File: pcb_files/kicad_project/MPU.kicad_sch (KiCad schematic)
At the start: 12 parts, among them U2 MPU-6500

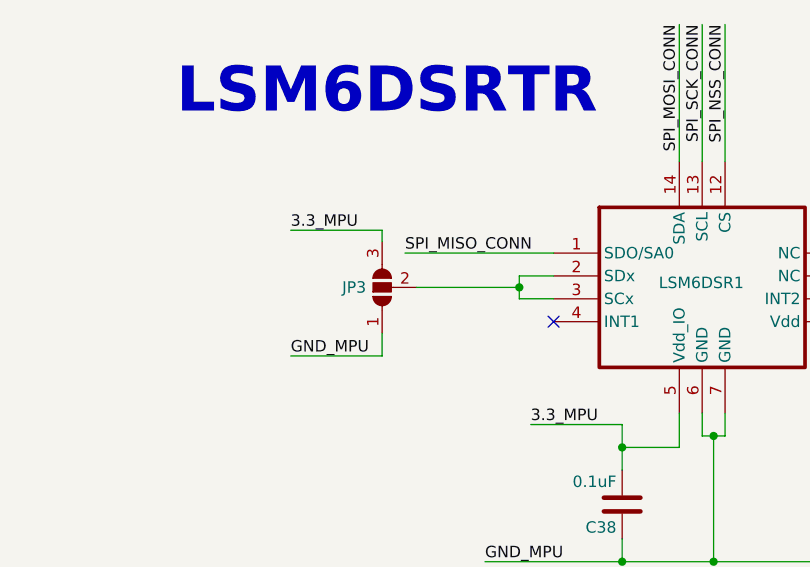
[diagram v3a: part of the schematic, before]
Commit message: Corrige errores de esquematico, crea las PCBs auxiliares, y posiciona todos los elementos para comenzar el ruteado.
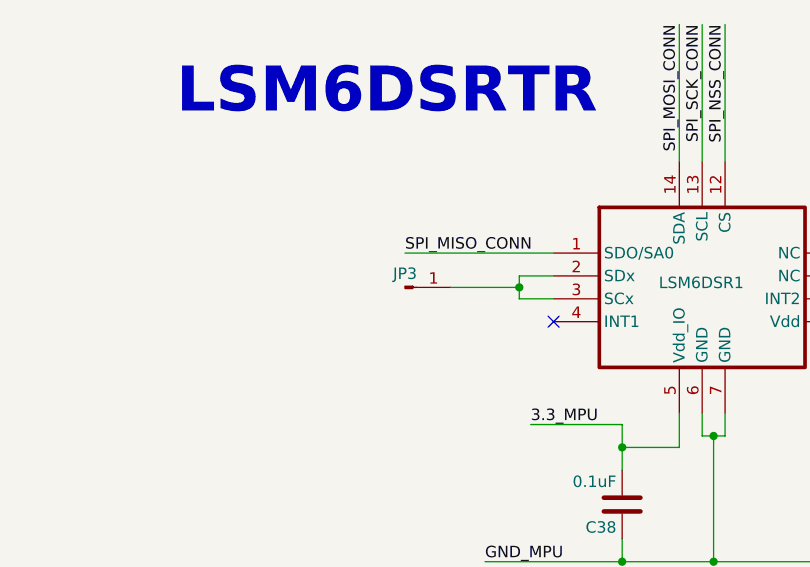
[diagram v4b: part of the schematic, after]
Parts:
- removed JP3: SolderJumper_3_Open, Jumper:SolderJumper-3_P1.3mm_Open_RoundedPad1.0x1.5mm, symbol Jumper:SolderJumper_3_Open
- added JP3: Conn_01x01_Pin, custom_footprints:Generic_simple_1x_SMD_pin, symbol Connector:Conn_01x01_Pin
- DATA_MPU2, DATA_MPU3: footprint custom_footprints:1x05 Pad -> custom_footprints:ZoroBot3_Data_MPU
- LSM6DSR1: footprint Sensor_Motion:Analog_LGA-16_3.25x3mm_P0.5mm_LayoutBorder3x5y -> Package_LGA:Bosch_LGA-14_3x2.5mm_P0.5mm
- POWER_MPU2, POWER_MPU3: footprint custom_footprints:1x05 Pad -> custom_footprints:ZoroBot3_Power_MPU
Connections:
- net at LSM6DSR1.2 (SDx), LSM6DSR1.3 (SCx): now also JP3.1 (Pin_1)
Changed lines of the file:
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@@
-	(wire
-		(pts
-			(xy 170.18 100.33) (xy 180.34 100.33)
-		)
-		(stroke
-			(width 0)
-			(type default)
-		)
-	)
 	(wire
 		(pts
@@
 	(wire
 		(pts
-			(xy 180.34 100.33) (xy 180.34 97.79)
-		)
-		(stroke
-			(width 0)
-			(type default)
-		)
-	)
-	(wire
-		(pts
 			(xy 217.17 109.22) (xy 217.17 123.19)
 		)
@@
 	(wire
 		(pts
-			(xy 180.34 86.36) (xy 180.34 87.63)
-		)
-		(stroke
-			(width 0)
-			(type default)
-		)
-	)
-	(wire
-		(pts
 			(xy 97.79 114.3) (xy 107.95 114.3)
 		)
@@
 	(wire
 		(pts
-			(xy 184.15 92.71) (xy 195.58 92.71)
+			(xy 187.96 92.71) (xy 195.58 92.71)
 		)
 		(stroke
@@
 		(pts
 			(xy 213.36 78.74) (xy 213.36 63.5)
-		)
-		(stroke
-			(width 0)
-			(type default)
-		)
-	)
-	(wire
-		(pts
-			(xy 180.34 86.36) (xy 170.18 86.36)
 		)
 		(stroke
@@
 		)
 	)
-	(label "3.3_MPU"
-		(at 170.18 86.36 0)
-		(fields_autoplaced yes)
-		(effects
-			(font
-				(size 1.27 1.27)
-			)
-			(justify left bottom)
-		)
-	)
 	(label "SPI_MOSI_CONN"
 		(at 142.24 128.27 180)
@@
 			)
 			(justify right bottom)
-		)
-	)
-	(label "GND_MPU"
-		(at 170.18 100.33 0)
-		(fields_autoplaced yes)
-		(effects
-			(font
-				(size 1.27 1.27)
-			)
-			(justify left bottom)
 		)
 	)
@@
 			)
 		)
-		(property "Footprint" "Sensor_Motion:Analog_LGA-16_3.25x3mm_P0.5mm_LayoutBorder3x5y"
+		(property "Footprint" "Package_LGA:Bosch_LGA-14_3x2.5mm_P0.5mm"
 			(at 215.9 93.98 0)
 			(effects
@@
 			)
 		)
-		(property "Footprint" "custom_footprints:1x05 Pad"
+		(property "Footprint" "custom_footprints:ZoroBot3_Power_MPU"
 			(at 120.65 115.57 0)
 			(effects
@@
 			)
 		)
-		(property "Footprint" "custom_footprints:1x05 Pad"
+		(property "Footprint" "custom_footprints:ZoroBot3_Data_MPU"
 			(at 248.92 127 0)
 			(effects
@@
 			)
 		)
-		(property "Footprint" "custom_footprints:1x05 Pad"
+		(property "Footprint" "custom_footprints:ZoroBot3_Data_MPU"
 			(at 120.65 128.27 0)
 			(effects
@@
 	)
 	(symbol
+		(lib_id "Connector:Conn_01x01_Pin")
+		(at 182.88 92.71 0)
+		(unit 1)
+		(exclude_from_sim no)
+		(in_bom yes)
+		(on_board yes)
+		(dnp no)
+		(property "Reference" "JP3"
+			(at 182.88 91.186 0)
+			(effects
+				(font
+					(size 1.27 1.27)
+				)
+			)
+		)
+		(property "Value" "Conn_01x01_Pin"
+			(at 183.642 93.98 0)
+			(effects
+				(font
+					(size 1.27 1.27)
+				)
+				(hide yes)
+			)
+		)
+		(property "Footprint" "custom_footprints:Generic_simple_1x_SMD_pin"
+			(at 182.88 92.71 0)
+			(effects
+				(font
+					(size 1.27 1.27)
+				)
+				(hide yes)
+			)
+		)
+		(property "Datasheet" "~"
+			(at 182.88 92.71 0)
+			(effects
+				(font
+					(size 1.27 1.27)
+				)
+				(hide yes)
+			)
+		)
+		(property "Description" "Generic connector, single row, 01x01, script generated"
+			(at 182.88 92.71 0)
+			(effects
+				(font
+					(size 1.27 1.27)
+				)
+				(hide yes)
+			)
+		)
+		(pin "1"
+		)
+		(instances
+			(project ""
+				(path "/38e8b839-c362-4120-bbf7-582efa82e48d/9d49d3a6-8e33-4528-aef9-1bba3efb9fbc"
+					(reference "JP3")
+					(unit 1)
+				)
+			)
+		)
+	)
+	(symbol
 		(lib_id "Device:C")
 		(at 207.01 116.84 180)
@@
 				(path "/38e8b839-c362-4120-bbf7-582efa82e48d/9d49d3a6-8e33-4528-aef9-1bba3efb9fbc"
 					(reference "C38")
-					(unit 1)
-				)
-			)
-		)
-	)
-	(symbol
-		(lib_id "Jumper:SolderJumper_3_Open")
-		(at 180.34 92.71 90)
-		(unit 1)
-		(exclude_from_sim yes)
-		(in_bom no)
-		(on_board yes)
-		(dnp no)
-		(property "Reference" "JP3"
-			(at 178.562 92.71 90)
-			(effects
-				(font
-					(size 1.27 1.27)
-				)
-				(justify left)
-			)
-		)
-		(property "Value" "SolderJumper_3_Open"
-			(at 173.736 102.616 0)
-			(effects
-				(font
-					(size 1.27 1.27)
-				)
-				(justify left)
-				(hide yes)
-			)
-		)
-		(property "Footprint" "Jumper:SolderJumper-3_P1.3mm_Open_RoundedPad1.0x1.5mm"
-			(at 180.34 92.71 0)
-			(effects
-				(font
-					(size 1.27 1.27)
-				)
-				(hide yes)
-			)
-		)
-		(property "Datasheet" "~"
-			(at 180.34 92.71 0)
-			(effects
-				(font
-					(size 1.27 1.27)
-				)
-				(hide yes)
-			)
-		)
-		(property "Description" "Solder Jumper, 3-pole, open"
-			(at 180.34 92.71 0)
-			(effects
-				(font
-					(size 1.27 1.27)
-				)
-				(hide yes)
-			)
-		)
-		(pin "3"
-		)
-		(pin "1"
-		)
-		(pin "2"
-		)
-		(instances
-			(project "ZoroBot3"
-				(path "/38e8b839-c362-4120-bbf7-582efa82e48d/9d49d3a6-8e33-4528-aef9-1bba3efb9fbc"
-					(reference "JP3")
 					(unit 1)
 				)
@@
 			)
 		)
-		(property "Footprint" "custom_footprints:1x05 Pad"
+		(property "Footprint" "custom_footprints:ZoroBot3_Power_MPU"
 			(at 248.92 114.3 0)
 			(effects

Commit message: Finaliza el diseño de la PCB de ZoroBot3 Rebuild y añade gerbers y BOM
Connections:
- net 3.3_MPU renamed 3.3_MPU_A
- net 3.3_MPU_A: no longer C37.2, C38.2, LSM6DSR1.5 (Vdd_IO), LSM6DSR1.8 (Vdd), POWER_MPU2.2 (Pin_2)
- net GND_MPU renamed GND_MPU_A
- net GND_MPU_A: no longer C37.1, C38.1, LSM6DSR1.6 (GND), LSM6DSR1.7 (GND), POWER_MPU2.1 (Pin_1)
- net SPI_MISO_CONN renamed SPI_MISO_CONN_A
- net SPI_MISO_CONN_A: no longer DATA_MPU2.1 (Pin_1), LSM6DSR1.1 (SDO/SA0)
- net SPI_MOSI_CONN renamed SPI_MOSI_CONN_A
- net SPI_MOSI_CONN_A: no longer DATA_MPU2.2 (Pin_2), LSM6DSR1.14 (SDA)
- net SPI_NSS_CONN renamed SPI_NSS_CONN_A
- net SPI_NSS_CONN_A: no longer DATA_MPU2.4 (Pin_4), LSM6DSR1.12 (CS)
- net SPI_SCK_CONN renamed SPI_SCK_CONN_A
- net SPI_SCK_CONN_A: no longer DATA_MPU2.3 (Pin_3), LSM6DSR1.13 (SCL)
- new net 3.3_MPU_B: C37.2, C38.2, LSM6DSR1.5 (Vdd_IO), LSM6DSR1.8 (Vdd), POWER_MPU2.2 (Pin_2)
- new net GND_MPU_B: C37.1, C38.1, LSM6DSR1.6 (GND), LSM6DSR1.7 (GND), POWER_MPU2.1 (Pin_1)
- new net SPI_MISO_CONN_B: DATA_MPU2.1 (Pin_1), LSM6DSR1.1 (SDO/SA0)
- new net SPI_MOSI_CONN_B: DATA_MPU2.2 (Pin_2), LSM6DSR1.14 (SDA)
- new net SPI_NSS_CONN_B: DATA_MPU2.4 (Pin_4), LSM6DSR1.12 (CS)
- new net SPI_SCK_CONN_B: DATA_MPU2.3 (Pin_3), LSM6DSR1.13 (SCL)
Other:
- moved on the sheet: C39, JP3
